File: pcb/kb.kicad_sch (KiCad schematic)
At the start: 434 parts, among them SW1 RotaryEncoder_Switch

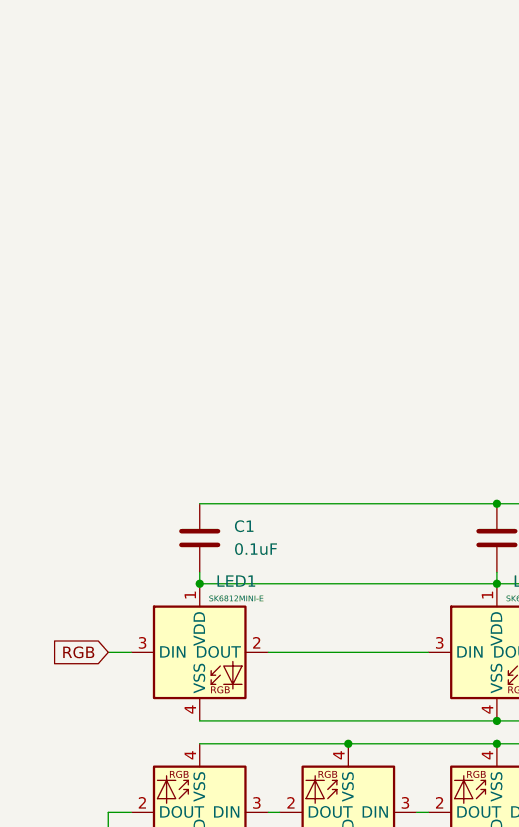
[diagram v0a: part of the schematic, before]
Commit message: add level shifter
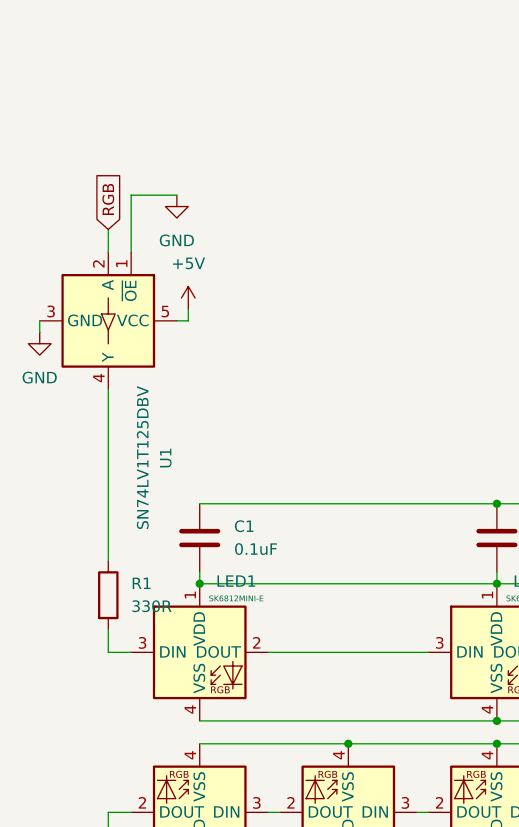
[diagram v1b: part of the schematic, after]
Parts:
- added R1: 330R, Resistor_SMD:R_0603_1608Metric_Pad0.98x0.95mm_HandSolder, symbol Device:R
- added U1: SN74LV1T125DBV, Package_TO_SOT_SMD:SOT-23-5_HandSoldering, symbol Logic_LevelTranslator:SN74LV1T125DBV
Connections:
- net +5V: now also U1.5 (VCC)
- net GND: now also U1.1 (~{OE}), U1.3 (GND)
- net RGB: now also U1.2 (A); no longer LED1.3 (DIN)
- new net: R1.1, U1.4 (Y)
- new net: LED1.3 (DIN), R1.2

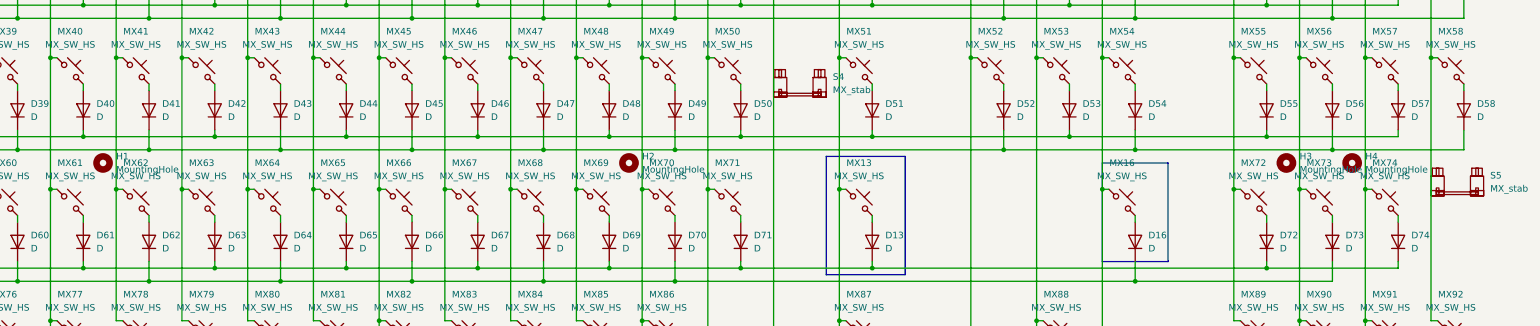
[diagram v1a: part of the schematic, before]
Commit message: Finalise PCB + Add PCB production files
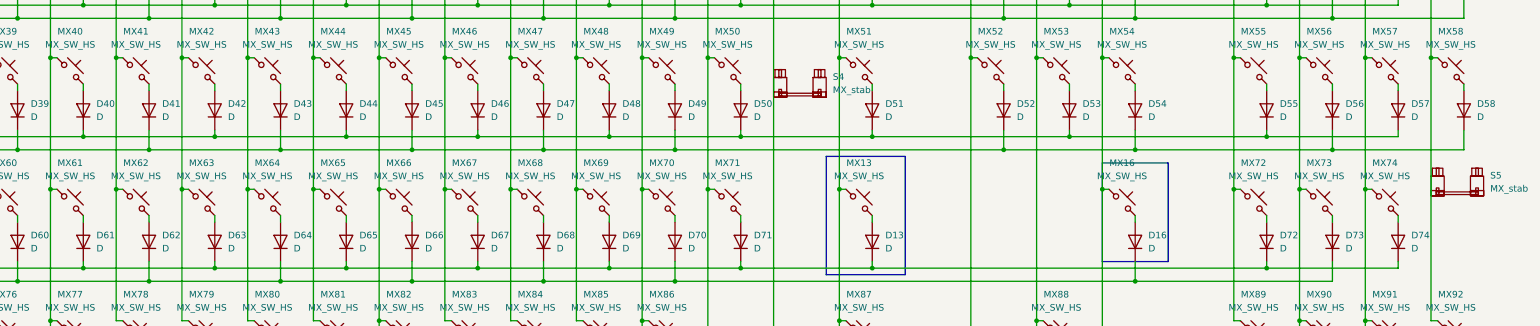
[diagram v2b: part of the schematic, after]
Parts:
- removed H1, H2, H3, H4: MountingHole, MountingHole:MountingHole_2.2mm_M2_DIN965, symbol Mechanical:MountingHole

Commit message: update pcb files
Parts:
- R1: footprint Resistor_SMD:R_0603_1608Metric_Pad0.98x0.95mm_HandSolder -> Resistor_SMD:R_0805_2012Metric_Pad1.20x1.40mm_HandSolder
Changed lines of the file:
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@@
 			)
 		)
-		(property "Footprint" "Resistor_SMD:R_0603_1608Metric_Pad0.98x0.95mm_HandSolder"
+		(property "Footprint" "Resistor_SMD:R_0805_2012Metric_Pad1.20x1.40mm_HandSolder"
 			(at 19.812 228.6 90)
 			(effects
